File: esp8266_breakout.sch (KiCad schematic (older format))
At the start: 39 parts, among them CON1 USB-MICRO-B2, P1 CONN_12, Q1 MOS_P, Q2 MOS_N, SW1 SW_PUSH, U1 NCP1117LP, U2 ESP8266-3, U3 FT230XS

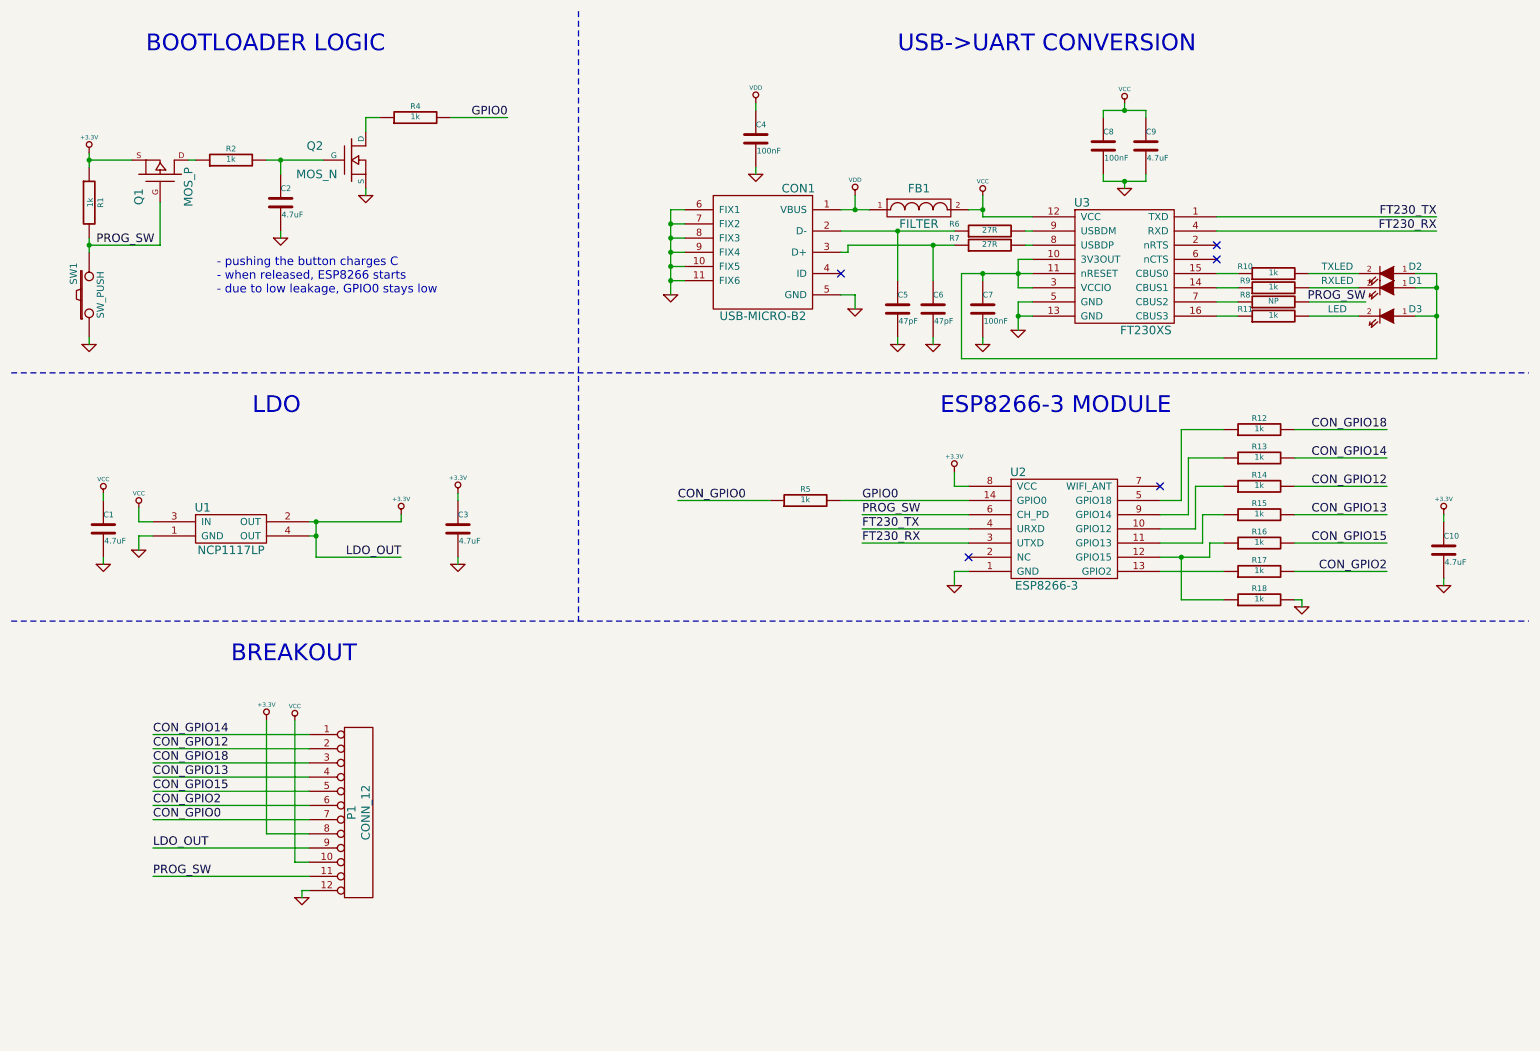
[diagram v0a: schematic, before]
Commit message: Added ufl connector cleaned up schematic
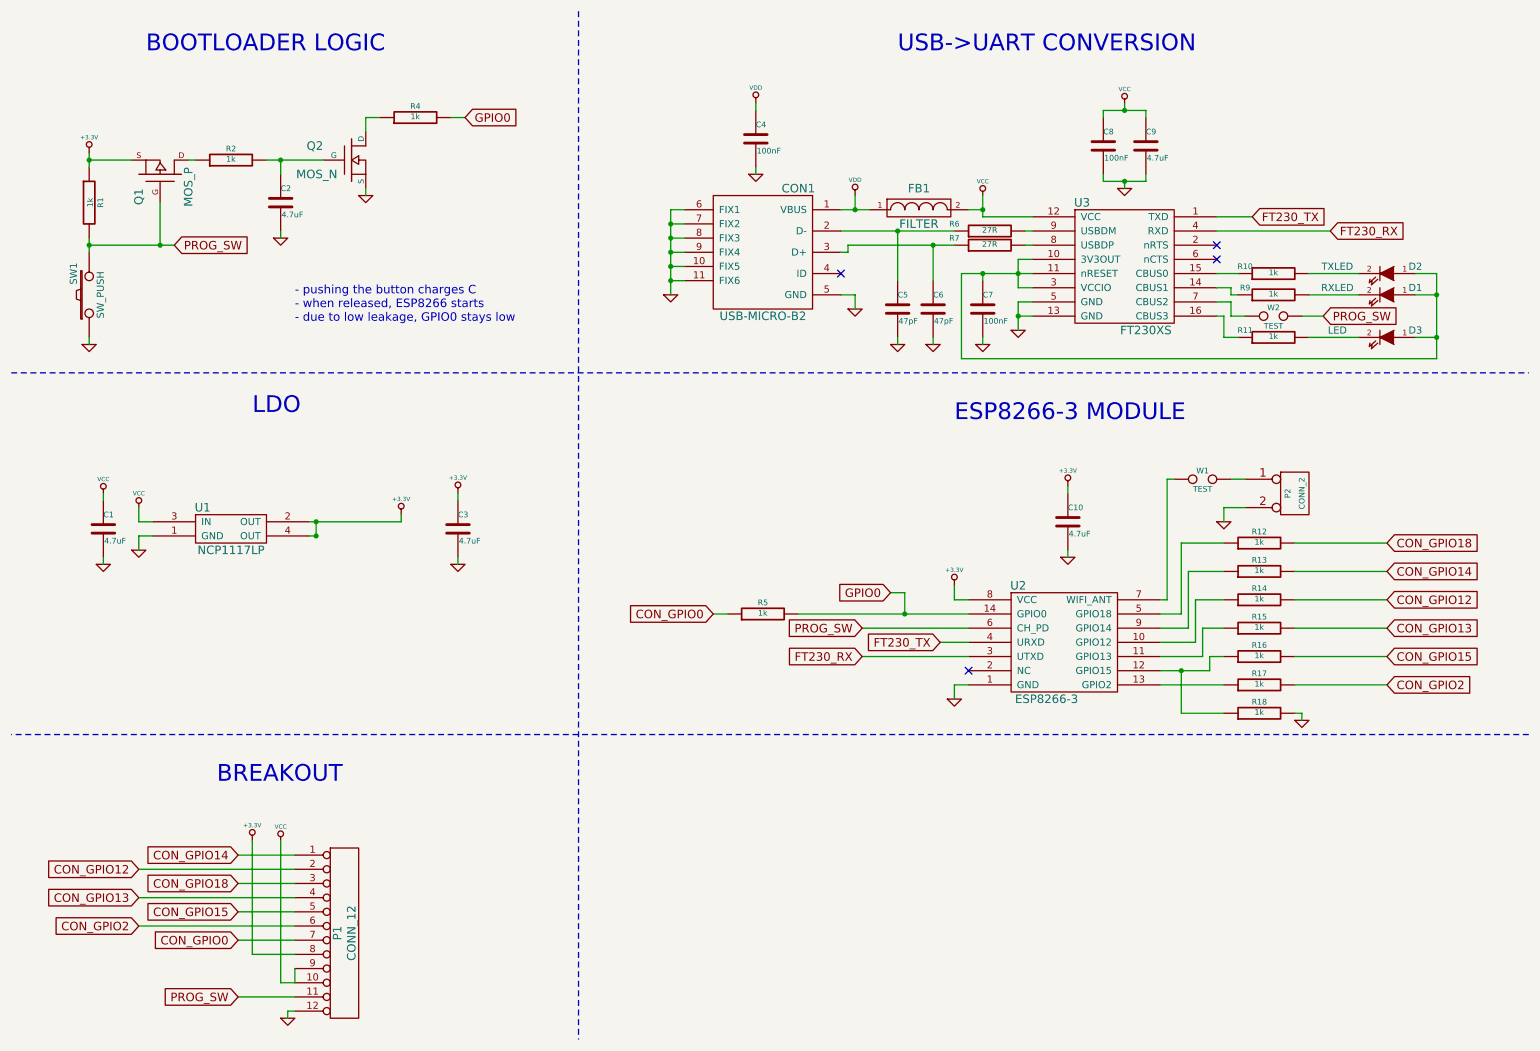
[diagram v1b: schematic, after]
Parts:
- removed R8: NP, ~, symbol R
- added P2: CONN_2, ~, symbol CONN_2
- added W1, W2: TEST, ~, symbol TEST
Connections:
- net +3.3V: no longer P1.9 (P9)
- net GND: now also P2.2 (PM)
- net PROG_SW: now also W2.2
- net VCC: now also P1.9 (P9)
- net at U2.7 (WIFI_ANT): now also W1.1
- net at U3.7 (CBUS2): now also W2.1
- new net: P2.1 (P1), W1.2
- no-connect marks 5 -> 4
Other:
- moved on the sheet: C10, D1, D3, P1, R11, R12, R13, R14, R15, R16, R17, R18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
